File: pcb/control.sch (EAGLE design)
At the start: 74 parts, among them J1 USB-C, J101 MICROSD, J2 2X5, J301 PCC-SMP, J302 3X1_2.54, J304 PCC-SMP, J306 4P-PC-FAN, J307 2X1_2.54, M201 HM-11, Q201 BC817-40, Q202 BC817-40, Q305 BC817-40, Q306 BC817-40, U1 EFM32GG11B4XX_QFN64, U102 SST26VF064B, U2 74LVC1G17, U204 ER-TFT035-6BOT, U205 CP2102N, U301 MCP9600, U302 MCP9600, Y101 8MHz, Y102 32.768KHz

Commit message: pcb v2 done
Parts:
- removed B201: (no value), Eletromechanical > Buzzer:PKLCS1212E2400-R1
- removed C101, C102, C103, C104, C105, C110, C111, C205, C206, C208, C301, C302, C303: 100n, Passive Components > Capacitors > Multilayer Ceramic Capacitors MLCC:MLCC0603
- removed C106, C108, C109: 1u, Passive Components > Capacitors > Multilayer Ceramic Capacitors MLCC:MLCC0603
- removed C207, C209: (no value), Passive Components > Capacitors > Multilayer Ceramic Capacitors MLCC:MLCC0603
- removed D207, D208, D209: LED0603, Opto-electronics > LED Emitters:LED0603
- removed J101: MICROSD, Connectors > card socket:MICROSD
- removed J301, J304: PCC-SMP, Connectors > Other:PCC-SMP
- removed J302: 3X1_2.54, Connectors > Header:3X1_2.54
- removed J306: 4P-PC-FAN, Thermal Management > Fans & Blowers:4P-PC-FAN
- removed J307: 2X1_2.54, Connectors > Header:2X1_2.54
- removed M201: HM-11, Embedded > BLE Module:HM-11
- removed Q201, Q202, Q305, Q306: BC817-40, Semiconductors > Discrete Semiconductors > Transistors > Bipolar Transistors - BJT:BC817-40
- removed R101, R102, R103, R104: 4k7, Passive Components > Resistors > Chip Resistors:RESISTOR0603
- removed R105, R106: (no value), Passive Components > Resistors > Chip Resistors:RESISTOR0603
- removed R203, R212, R318, R319: 1k, Passive Components > Resistors > Chip Resistors:RESISTOR0603
- removed R204, R205, R209, R210, R211: 220, Passive Components > Resistors > Chip Resistors:RESISTOR0603
- removed R206, R213, R320, R321, R326: 100k, Passive Components > Resistors > Chip Resistors:RESISTOR0603
- removed R207: 22.1k, Passive Components > Resistors > Chip Resistors:RESISTOR0603
- removed R208: 47.5k, Passive Components > Resistors > Chip Resistors:RESISTOR0603
- removed R214, R323: 100, Passive Components > Resistors > Chip Resistors:RESISTOR0603
- removed R317: 33k, Passive Components > Resistors > Chip Resistors:RESISTOR0603
- removed SW101: (no value), Eletromechanical > Switches > Tactile Switches:PUSH_BUTTON
- removed U102: SST26VF064B, Semiconductors > Integrated Circuits - ICs > Memory ICs > Flash:SST26VF064B
- removed U204: ER-TFT035-6BOT, Opto-electronics > Displays:ER-TFT035-6BOT
- removed U205: CP2102N, Semiconductors > Integrated Circuits - ICs > Interface ICs > USB Interface IC:CP2102N
- removed U301, U302: MCP9600, Sensors > Temperature Sensors:MCP9600
- removed Y101: 8MHz, Passive Components > Frequency Control & Timing Devices > Crystals:CRYSTALNX5032GA
- removed Y102: 32.768KHz, Passive Components > Frequency Control & Timing Devices > Crystals:CRYSTALCM200S
- added B1: (no value), Eletromechanical > Buzzer:PKLCS1212E2400-R1
- added C1, C4: 10u, Passive Components > Capacitors > Multilayer Ceramic Capacitors MLCC:MLCC0603_MINI
- added C10, C12, C13, C16, C17, C18, C19, C2, C20, C22, C23, C24, C3, C5, C8, C9: 100n, Passive Components > Capacitors > Multilayer Ceramic Capacitors MLCC:MLCC0603
- added C11: (no value), Passive Components > Capacitors > Aluminium Electrolytic Capacitors:CAPACITOR_ELD
- added C14, C15: (no value), Passive Components > Capacitors > Multilayer Ceramic Capacitors MLCC:MLCC0603
- added C25: 4u7, Passive Components > Capacitors > Multilayer Ceramic Capacitors MLCC:MLCC0603
- added C26: 10u, Passive Components > Capacitors > Multilayer Ceramic Capacitors MLCC:MLCC0603
- added C27: 1u, Passive Components > Capacitors > Multilayer Ceramic Capacitors MLCC:MLCC0603
- added C6: 220u, Passive Components > Capacitors > Aluminium Electrolytic Capacitors:CAPACITOR_ELD
- added C7: 470p, Passive Components > Capacitors > Multilayer Ceramic Capacitors MLCC:MLCC0603
- added D10, D11, D12, D13, D14, D7, D8, D9: SK9822, Opto-electronics > LED Emitters:SK9822
- added D2, D5, D6: LED0603, Opto-electronics > LED Emitters:LED0603
- added D3: SMAJ36A, Circuit Protection > ESD Suppressors \ TVS Diodes:SMAJ36A
- added D4: SP0503BAHT, Circuit Protection > ESD Suppressors \ TVS Diodes:SP0503BAHT
- added GND: (no value), Circuit Protection > Resettable Fuses - PPTC:PTC1812
- added J10: USB-C, Connectors > USB:USB-C
- added J3: PCC-SMP, Connectors > Other:PCC-SMP
- added J4: MICROSD, Connectors > card socket:MICROSD
- added J5, J8, J9: 2EDG-2P, Connectors > Other:2EDG-2P
- added J6: 3X1_2.54, Connectors > Header:3X1_2.54
- added J7: 4P-PC-FAN, Thermal Management > Fans & Blowers:4P-PC-FAN
- added L1: 6.8uH, Passive Components > Inductors, Chokes & Coils:INDUCTOR_1207
- added M1: HM-11, Embedded > BLE Module:HM-11
- added Q1, Q2, Q3, Q4: BC817-40, Semiconductors > Discrete Semiconductors > Transistors > Bipolar Transistors - BJT:BC817-40
- added R10, R24, R26, R29, R32: 220, Passive Components > Resistors > Chip Resistors:RESISTOR0603
- added R11, R3: (no value), Passive Components > Resistors > Chip Resistors:RESISTOR0603
- added R12, R13, R14, R15: 4k7, Passive Components > Resistors > Chip Resistors:RESISTOR0603
- added R16: 33k, Passive Components > Resistors > Chip Resistors:RESISTOR0603
- added R17, R18, R19, R25, R27: 1k, Passive Components > Resistors > Chip Resistors:RESISTOR0603
- added R20, R21, R22, R28, R35, R5: 100k, Passive Components > Resistors > Chip Resistors:RESISTOR0603
- added R23, R4: 100, Passive Components > Resistors > Chip Resistors:RESISTOR0603
- added R30: 22.1k, Passive Components > Resistors > Chip Resistors:RESISTOR0603
- added R31: 47.5k, Passive Components > Resistors > Chip Resistors:RESISTOR0603
- added R33, R34: 5.1k, Passive Components > Resistors > Chip Resistors:RESISTOR0603
- added R6: 3k01, Passive Components > Resistors > Chip Resistors:RESISTOR0603
- added R7: 953, Passive Components > Resistors > Chip Resistors:RESISTOR0603
- added R8: 300k, Passive Components > Resistors > Chip Resistors:RESISTOR0603
- added R9: 47k, Passive Components > Resistors > Chip Resistors:RESISTOR0603
- added SW1: (no value), Eletromechanical > Switches > Tactile Switches:PUSH_BUTTON
- added U10: EFM32GG11B4XX_Q100, Semiconductors > Embedded Processors & Controllers > Microcontrollers - MCU:EFM32GG11B4XX_Q100
- added U3: SST26VF064B, Semiconductors > Integrated Circuits - ICs > Memory ICs > Flash:SST26VF064B
- added U4: MCP9600, Sensors > Temperature Sensors:MCP9600
- added U5, U8, U9: 74LVC1G17, Semiconductors > Integrated Circuits - ICs > Logic ICs > Logic Gates:74LVC1G17
- added U6: CP2102N, Semiconductors > Integrated Circuits - ICs > Interface ICs > USB Interface IC:CP2102N
- added U7: ER-TFT035-6BOT, Opto-electronics > Displays:ER-TFT035-6BOT
- added Y1: 8MHz, Passive Components > Frequency Control & Timing Devices > Crystals:CRYSTALNX5032GA
- added Y2: 32.768KHz, Passive Components > Frequency Control & Timing Devices > Crystals:CRYSTALCM200S
- D1: value SP0503BAHT -> SK54L; device Circuit Protection > ESD Suppressors \ TVS Diodes:SP0503BAHT -> Semiconductors > Discrete Semiconductors > Diodes & Rectifiers > Schottky Diodes & Rectifiers:SK54L
- J1: value USB-C -> PCC-SMP; device Connectors > USB:USB-C -> Connectors > Other:PCC-SMP
- J2: value 2X5 -> 2X1_2.54; device Connectors > Header > Shrouded:2X5 -> Connectors > Header:2X1_2.54
- R1: value 1k -> 10M
- U1: value EFM32GG11B4XX_QFN64 -> MIC4682; device Semiconductors > Embedded Processors & Controllers > Microcontrollers - MCU:EFM32GG11B4XX_QFN64 -> Power > Switching Controllers:MIC4682
- U2: value 74LVC1G17 -> MCP9600; device Semiconductors > Integrated Circuits - ICs > Logic ICs > Logic Gates:74LVC1G17 -> Sensors > Temperature Sensors:MCP9600
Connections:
- new net !5V-ERR: U10.PD2
- new net 5V-SENSE: U10.PD4
- new net N$10: D8.SDO@1, D9.SDI@3
- new net N$11: D8.CLKO@6, D9.CLKI@4
- new net N$12: D10.SDI@3, D9.SDO@1
- new net N$14: D10.CLKI@4, D9.CLKO@6
- new net N$20: D10.SDO@1, D11.SDI@3
- new net N$21: D10.CLKO@6, D11.CLKI@4
- new net N$22: D11.SDO@1, D12.SDI@3
- new net N$23: D11.CLKO@6, D12.CLKI@4
- new net N$24: D12.SDO@1, D13.SDI@3
- new net N$26: D12.CLKO@6, D13.CLKI@4
- new net N$27: D13.SDO@1, D14.SDI@3
- new net N$28: D13.CLKO@6, D14.CLKI@4
- new net N$30: GND.2, J5.1.S
- new net N$31: D1.C, L1.P$1, U1.SW
- new net N$32: R6.P$1, R7.P$2, U1.FB
- new net N$34: R1.P$1, R2.P$2, U1.ISET
- new net N$5: J10.CC1@A5, R33.P$2
- new net N$6: D7.SDO@1, D8.SDI@3
- new net N$7: D7.CLKI@4, U9.1.Y
- new net N$8: D7.SDI@3, U8.1.Y
- new net N$9: D7.CLKO@6, D8.CLKI@4
- new net US0-LED-MOSI: U10.PE7, U8.1.A
- new net US0-LED-SCK: U10.PE5, U9.1.A
- new net VIN-SENSE: C7.P$1, R8.P$1, R9.P$2, U10.PD0
- net !RESET: now also SW1.1, SW1.2, U10.!RESET; no longer SW101.1, SW101.2, U1.!RESET@20
- net !TFT_RESET: now also U10.PB5, U7.!RESET; no longer U204.!RESET
- net !TTFT-IRQ: now also U10.PB3, U7.X-/!IRQ!; no longer U204.X-/!IRQ!
- net !TTFT-RST: now also U10.PB6, U7.Y-/!RST!; no longer U204.Y-/!RST!
- net 12V: now also C1.P$1, C11.AN, D3.C, GND.1, J7-12VDC.S, R1.P$2, R22.P$2, R8.P$2, U1.IN; no longer J2-1.S, J2-3.S, J306-12VDC.S, R321.P$2
- net 3.3V: now also C10.P$1, C12.P$1, C13.P$1, C14.P$1, C15.P$1, C16.P$1, C17.P$1, C18.P$1, C19.P$1, C2.P$1, C20.P$1, C22.P$1, C24.P$1, C25.P$1, C5.P$1, C8.P$1, C9.P$1, J4.4, M1.VCC@9, R11.P$2, R12.P$2, R13.P$2, R14.P$2, R15.P$2, R24.P$1, R26.P$1, R28.P$2, R3.P$2, R35.P$2, R5.P$2, U10.AVDD@0, U10.AVDD@1, U10.DVDD, U10.IOVDD0@0, U10.IOVDD0@1, U10.IOVDD0@2, U10.IOVDD0@3, U10.IOVDD0@4, U10.VREGO, U2.VDD@8, U3.VCC, U4.ADDR@16, U4.VDD@8, U6.VDD@6, U6.VIO@5, U6.VREGIN@7, U7.!RD, U7.IM0, U7.IM1, U7.IM2, U7.VCI, U7.VDDI@0, U7.VDDI@1; no longer C101.P$1, C102.P$1, C103.P$1, C104.P$1, C105.P$1, C106.P$1, C110.P$1, C111.P$1, C205.P$1, C206.P$1, C207.P$1, C208.P$1, C209.P$1, C301.P$1, C302.P$1, J101.4, M201.VCC@9, R101.P$2, R102.P$2, R103.P$2, R104.P$2, R105.P$2, R106.P$2, R206.P$2, R209.P$1, R210.P$1, R326.P$2, U1.AVDD@23, U1.AVDD@27, U1.DVDD@39, U1.IOVDD0@26, U1.IOVDD0@55, U1.IOVDD0@8, U1.VREGO@46, U102.VCC, U204.!RD, U204.IM0, U204.IM1, U204.IM2, U204.VCI, U204.VDDI@0, U204.VDDI@1, U205.VDD@6, U205.VIO@5, U205.VREGIN@7, U301.VDD@8, U302.ADDR@16, U302.VDD@8
- net 5V: now also C23.P$1, C26.P$1, C4.P$1, C6.AN, D10.VDD@5, D11.VDD@5, D12.VDD@5, D13.VDD@5, D14.VDD@5, D7.VDD@5, D8.VDD@5, D9.VDD@5, J6-2.S, L1.P$2, R21.P$2, R23.P$2, R6.P$2, U10.VBUS, U10.VREGI, U5.PW.VCC, U7.LEDA, U8.PW.VCC, U9.PW.VCC; no longer C108.P$1, J2-5.S, J2-7.S, J302-2.S, R213.P$2, R214.P$2, U1.VBUS@52, U1.VREGI@45, U2.PW.VCC, U204.LEDA
- net BLE-!RST: now also M1.!RST!@11, U10.PE0; no longer M201.!RST!@11
- net BLE-KEY: now also M1.PIO0@16, U10.PE1; no longer M201.PIO0@16
- net DECOUPLE: now also C27.P$1, U10.DECOUPLE; no longer C109.P$1, U1.DECOUPLE@40
- net DOOR-SW: now also C3.P$1, R4.P$2, U10.PC7; no longer C303.P$1, R323.P$2
- net GND: now also C1.P$2, C10.P$2, C11.CA, C12.P$2, C13.P$2, C14.P$2, C15.P$2, C16.P$2, C17.P$2, C18.P$2, C19.P$2, C2.P$2, C20.P$2, C22.P$2, C23.P$2, C24.P$2, C25.P$2, C26.P$2, C27.P$2, C3.P$2, C4.P$2, C5.P$2, C6.CA, C7.P$2, C8.P$2, C9.P$2, D1.A, D10.GND@2, D11.GND@2, D12.GND@2, D13.GND@2, D14.GND@2, D2.CA, D3.A, D4.1, D7.GND@2, D8.GND@2, D9.GND@2, J1.BAR.S, J10.GND@A12,A1,B1,B12, J3.BAR.S, J4.6, J4.BODY@10, J5.2.S, J6-3.S, J8.2.S, J9.2.S, M1.GND@12, Q1.EM2, Q2.EM2, Q3.EM2, Q4.EM2, R16.P$1, R25.P$1, R31.P$1, R33.P$1, R34.P$1, R7.P$1, R9.P$1, SW1.3, SW1.4, U1.GND@1, U1.GND@2, U1.GND@3, U1.SHDN, U10.VSS@0, U10.VSS@1, U10.VSS@2, U10.VSS@3, U2.ADDR@16, U2.EP, U2.GND@1, U2.GND@10, U2.GND@13, U2.GND@17, U2.GND@18, U2.GND@3, U2.GND@5, U2.GND@6, U2.GND@7, U2.GND@9, U3.GND, U4.EP, U4.GND@1, U4.GND@10, U4.GND@13, U4.GND@17, U4.GND@18, U4.GND@3, U4.GND@5, U4.GND@6, U4.GND@7, U4.GND@9, U5.PW.GND, U6.GND@2, U6.GND@PAD, U7.DB0, U7.DB1, U7.DB10, U7.DB11, U7.DB12, U7.DB13, U7.DB14, U7.DB15, U7.DB16, U7.DB17, U7.DB2, U7.DB3, U7.DB4, U7.DB5, U7.DB6, U7.DB7, U7.DB8, U7.DB9, U7.DE, U7.DOTCLK, U7.GND@0, U7.GND@1, U7.GND@2, U7.GND@3, U7.HSYNC, U7.TE, U7.VSYNC, U8.PW.GND, U9.PW.GND; no longer C101.P$2, C102.P$2, C103.P$2, C104.P$2, C105.P$2, C106.P$2, C108.P$2, C109.P$2, C110.P$2, C111.P$2, C205.P$2, C206.P$2, C207.P$2, C208.P$2, C209.P$2, C301.P$2, C302.P$2, C303.P$2, D1.1, D208.CA, J1.GND@A12,A1,B1,B12, J101.6, J101.BODY@10, J2-4.S, J2-6.S, J2-8.S, J301.BAR.S, J302-3.S, J304.BAR.S, J307-2.S, M201.GND@12, Q201.EM2, Q202.EM2, Q305.EM2, Q306.EM2, R1.P$1, R208.P$1, R317.P$1, SW101.3, SW101.4, U1.VSS@65, U102.GND, U2.PW.GND, U204.DB0, U204.DB1, U204.DB10, U204.DB11, U204.DB12, U204.DB13, U204.DB14, U204.DB15, U204.DB16, U204.DB17, U204.DB2, U204.DB3, U204.DB4, U204.DB5, U204.DB6, U204.DB7, U204.DB8, U204.DB9, U204.DE, U204.DOTCLK, U204.GND@0, U204.GND@1, U204.GND@2, U204.GND@3, U204.HSYNC, U204.TE, U204.VSYNC, U205.GND@2, U205.GND@PAD, U301.ADDR@16, U301.EP, U301.GND@1, U301.GND@10, U301.GND@13, U301.GND@17, U301.GND@18, U301.GND@3, U301.GND@5, U301.GND@6, U301.GND@7, U301.GND@9, U302.EP, U302.GND@1, U302.GND@10, U302.GND@13, U302.GND@17, U302.GND@18, U302.GND@3, U302.GND@5, U302.GND@6, U302.GND@7, U302.GND@9
- net I2C0-SCL-SENS: now also R13.P$1, U10.PD7, U2.SCL@19, U4.SCL@19; no longer R102.P$1, U301.SCL@19, U302.SCL@19
- net I2C0-SDA-SENS: now also R12.P$1, U10.PD6, U2.SDA@20, U4.SDA@20; no longer R101.P$1, U301.SDA@20, U302.SDA@20
- net I2C1-SCL-TTFT: now also R15.P$1, U10.PB12, U7.X+/SCL; no longer R104.P$1, U204.X+/SCL
- net I2C1-SDA-TTFT: now also R14.P$1, U10.PB11, U7.Y+/SDA; no longer R103.P$1, U204.Y+/SDA
- net MAIN_HFXTAL_N: now also U10.PB13, Y1.1; no longer Y101.1
- net MAIN_HFXTAL_P: now also U10.PB14, Y1.2; no longer Y101.2
- net MAIN_LFXTAL_N: now also U10.PB8, Y2.2; no longer Y102.2
- net MAIN_LFXTAL_P: now also U10.PB7, Y2.1; no longer Y102.1
- net N$1: now also J2-1.S, R4.P$1, R5.P$1; no longer J307-1.S, R323.P$1, R326.P$1
- net N$13: now also D5.CA, U6.GPIO1-RXT@13; no longer D207.CA, U205.GPIO1-RXT@13
- net N$15: now also D6.CA, U6.GPIO0-TXT@14; no longer D209.CA, U205.GPIO0-TXT@14
- net N$16: now also D6.AN, R26.P$2; no longer D209.AN, R210.P$2
- net N$17: now also B1.B, Q1.C03, R21.P$1; no longer B201.B, Q202.C03, R213.P$1
- net N$18: now also Q1.BA1, R17.P$2; no longer Q202.BA1, R212.P$2
- net N$19: now also D5.AN, R24.P$2; no longer D207.AN, R209.P$2
- net N$2: now also J6-1.S, U5.1.Y; no longer J302-1.S, U2.1.Y
- net N$25: now also Q4.BA1, R27.P$2; no longer Q201.BA1, R203.P$2
- net N$3: now also J10.CC2@B5, R34.P$2; no longer J1.CC@A5,B5, R2.P$2
- net N$35: now also D2.AN, R10.P$2; no longer D208.AN, R211.P$2
- net N$36: now also M1.PIO1@15, R10.P$1; no longer M201.PIO1@15, R211.P$1
- net N$4: now also B1.A, R23.P$1; no longer B201.A, R214.P$1
- net N$56: now also Q3.BA1, R19.P$2; no longer Q306.BA1, R319.P$2
- net N$57: now also J7-GND.S, Q3.C03; no longer J306-GND.S, Q306.C03
- net N$58: now also Q2.BA1, R18.P$2; no longer Q305.BA1, R318.P$2
- net N$59: now also J7-CTRL.S, Q2.C03, R22.P$1; no longer J306-CTRL.S, Q305.C03, R321.P$1
- net N$64: now also J7-SENSE.S, R20.P$2; no longer J306-SENSE.S, R320.P$2
- net PRS-CH11-SSR-OUT: now also J9.1.S, U10.PD5; no longer J2-9.S
- net QSPI_CLK: now also U10.PF6, U3.SCK; no longer U102.SCK
- net QSPI_CS0: now also R3.P$1, U10.PF7, U3.!CS!; no longer R105.P$1, U102.!CS!
- net QSPI_D0: now also U10.PD9, U3.MOSI/IO0; no longer U102.MOSI/IO0
- net QSPI_D1: now also U10.PD10, U3.MISO/IO1; no longer U102.MISO/IO1
- net QSPI_D2: now also U10.PD11, U3.!WP!/IO2; no longer U102.!WP!/IO2
- net QSPI_D3: now also U10.PD12, U3.!HOLD!/IO3; no longer U102.!HOLD!/IO3
- net SDIO-CD: now also J4.CD@9, R11.P$1, U10.PF8; no longer J101.CD@9, R106.P$1
- net SDIO-CLK: now also J4.5, U10.PE13; no longer J101.5
- net SDIO-CMD: now also J4.3, U10.PE12; no longer J101.3
- net SDIO-DAT0: now also J4.7, U10.PE11; no longer J101.7
- net SDIO-DAT1: now also J4.8, U10.PE10; no longer J101.8
- net SDIO-DAT2: now also J4.1, U10.PE9; no longer J101.1
- net SDIO-DAT3: now also J4.2, U10.PE8; no longer J101.2
- net SWCLK: now also U10.PF0
- net SWDIO: now also U10.PF1
- net SWO: now also U10.PF2
- net TC_VIN0+: now also J1.T+.S, U2.VIN+@2; no longer J301.T+.S, U301.VIN+@2
- net TC_VIN0-: now also J1.T-.S, U2.VIN-@4; no longer J301.T-.S, U301.VIN-@4
- net TC_VIN1+: now also J3.T+.S, U4.VIN+@2; no longer J304.T+.S, U302.VIN+@2
- net TC_VIN1-: now also J3.T-.S, U4.VIN-@4; no longer J304.T-.S, U302.VIN-@4
- net TFT-DC: now also U10.PC1, U7.D/!C!; no longer U204.D/!C!
- net TFT-LEDK: now also Q4.C03, R29.P$1, R32.P$1; no longer Q201.C03, R204.P$1, R205.P$1
- net TFT-LEDK1: now also R29.P$2, U7.LEDK@0; no longer R204.P$2, U204.LEDK@0
- net TFT-LEDK2: now also R32.P$2, U7.LEDK@1; no longer R205.P$2, U204.LEDK@1
- net TIM0-CC2-BUZZ: now also R17.P$1, U10.PA8; no longer R212.P$1
- net TIM1-CC0-TFT-BL: now also R25.P$2, R27.P$1, U10.PB0; no longer R1.P$2, R203.P$1
- net TIM2-CC2FAN0-SNSE: now also R16.P$2, R20.P$1, U10.PC10; no longer R317.P$2, R320.P$1
- net TIM5-CC0-FAN0-GND: now also R19.P$1, U10.PC8; no longer R319.P$1
- net TIM5-CC1-FAN0-CTRL: now also R18.P$1, U10.PC9; no longer R318.P$1
- net U0RX-USB-TX: now also U10.PA4, U6.TXD@21; no longer U205.TXD@21
- net U0TX-USB-RX: now also U10.PA3, U6.RXD@20; no longer U205.RXD@20
- net U1RX-BLE-TX: now also M1.TX@2, U10.PE3; no longer M201.TX@2
- net U1TX-BLE-RX: now also M1.RX@4, U10.PE2; no longer M201.RX@4
- net UART_VBUS: now also R30.P$1, R31.P$2, U6.VBUS@8; no longer R207.P$1, R208.P$2, U205.VBUS@8
- net US2-CLK-TFT: now also U10.PC4, U7.!WR!/SCL; no longer U204.!WR!/SCL
- net US2-CS-TFT: now also R35.P$1, U10.PC5, U7.!CS; no longer R206.P$1, U204.!CS
- net US2-MISO-TFT: now also U10.PC3, U7.SDO; no longer U204.SDO
- net US2-MOSI-TFT: now also U10.PC2, U7.SDA; no longer U204.SDA
- net USB-RST: now also U10.PA2, U6.RSTB@9; no longer U205.RSTB@9
- net USB-SUS: now also U10.PA1, U6.SUSPEND@17; no longer U205.SUSPEND@17
- net USB-UART-D+: now also D4.3, J10.DP@A6,B6, U6.D+@3; no longer D1.3, J1.DP@A6,B6, U205.D+@3
- net USB-UART-D-: now also D4.2, J10.DN@A7,B7, U6.D-@4; no longer D1.2, J1.DN@A7,B7, U205.D-@4
- net V_USB: now also D4.4, J10.VBUS@B9,B4,A4,A9, R30.P$2; no longer D1.4, J1.VBUS@B9,B4,A4,A9, R207.P$2
- net WTIM1-CC1-ZERO-CROSS: now also J8.1.S, R28.P$1, U10.PE4; no longer J2-10.S
- net WTIM2-CC0-SERVO0-SIG: now also U10.PD3, U5.1.A; no longer U2.1.A

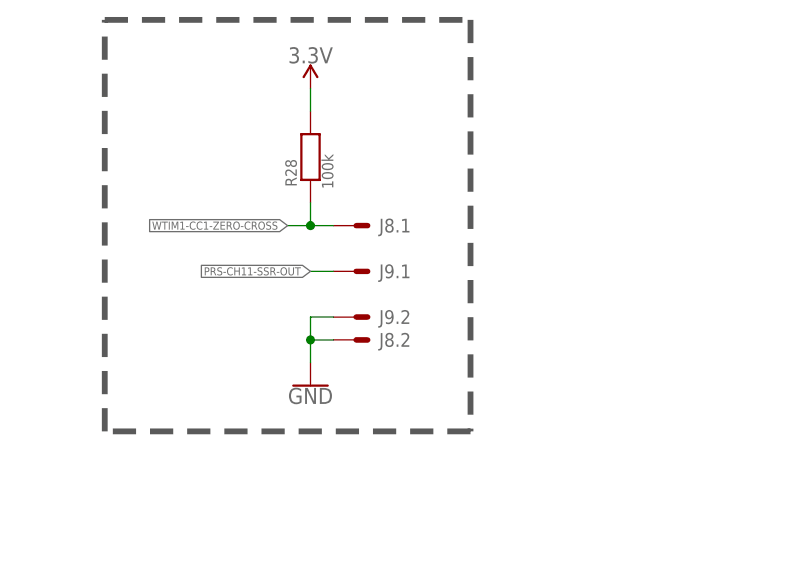
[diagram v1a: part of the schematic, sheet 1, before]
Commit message: finished silkscreen and ssr pcb
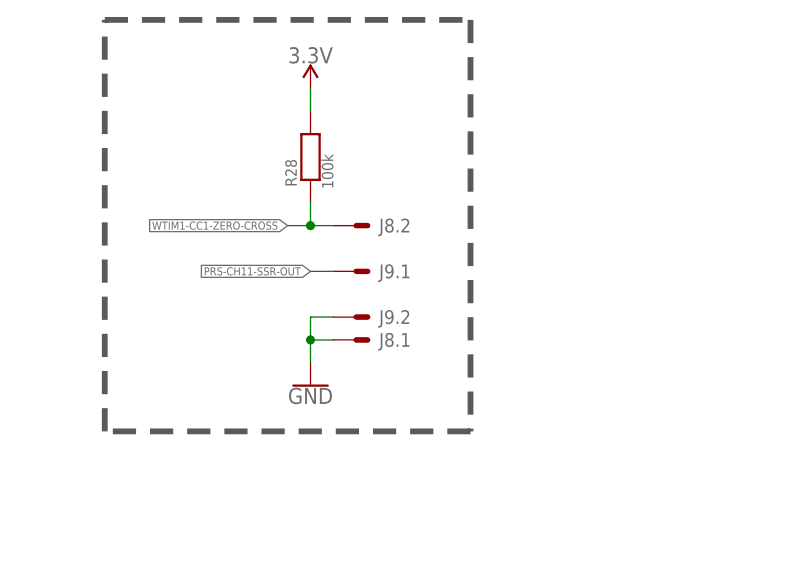
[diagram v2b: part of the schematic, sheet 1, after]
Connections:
- net GND: now also J8.1.S; no longer J8.2.S
- net WTIM1-CC1-ZERO-CROSS: now also J8.2.S; no longer J8.1.S
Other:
- moved on the sheet: J8.1, J8.2
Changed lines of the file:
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@@
 <attribute name="VALUE" x="462.28" y="-50.546" size="1.778" layer="96" align="bottom-center"/>
 </instance>
-<instance part="J8" gate=".1" x="612.14" y="-66.04" smashed="yes">
+<instance part="J8" gate=".1" x="612.14" y="-78.74" smashed="yes">
+<attribute name="NAME" x="614.68" y="-79.502" size="1.524" layer="95"/>
+</instance>
+<instance part="J8" gate=".2" x="612.14" y="-66.04" smashed="yes">
 <attribute name="NAME" x="614.68" y="-66.802" size="1.524" layer="95"/>
-</instance>
-<instance part="J8" gate=".2" x="612.14" y="-78.74" smashed="yes">
-<attribute name="NAME" x="614.68" y="-79.502" size="1.524" layer="95"/>
 </instance>
 <instance part="J9" gate=".1" x="612.14" y="-71.12" smashed="yes">
@@
 <pinref part="J9" gate=".2" pin="S"/>
 <wire x1="609.6" y1="-76.2" x2="607.06" y2="-76.2" width="0.1524" layer="91"/>
-<pinref part="J8" gate=".2" pin="S"/>
+<wire x1="607.06" y1="-76.2" x2="607.06" y2="-78.74" width="0.1524" layer="91"/>
+<pinref part="GND41" gate="1" pin="GND"/>
+<pinref part="J8" gate=".1" pin="S"/>
+<wire x1="607.06" y1="-78.74" x2="607.06" y2="-81.28" width="0.1524" layer="91"/>
 <wire x1="609.6" y1="-78.74" x2="607.06" y2="-78.74" width="0.1524" layer="91"/>
-<wire x1="607.06" y1="-78.74" x2="607.06" y2="-81.28" width="0.1524" layer="91"/>
-<wire x1="607.06" y1="-76.2" x2="607.06" y2="-78.74" width="0.1524" layer="91"/>
 <junction x="607.06" y="-78.74"/>
-<pinref part="GND41" gate="1" pin="GND"/>
 </segment>
 <segment>
@@
 <segment>
 <label x="604.52" y="-66.04" size="0.889" layer="95" rot="R180" xref="yes"/>
-<wire x1="609.6" y1="-66.04" x2="607.06" y2="-66.04" width="0.1524" layer="91"/>
-<pinref part="J8" gate=".1" pin="S"/>
 <pinref part="R28" gate="G$1" pin="P$1"/>
 <wire x1="607.06" y1="-66.04" x2="604.52" y2="-66.04" width="0.1524" layer="91"/>
 <wire x1="607.06" y1="-63.5" x2="607.06" y2="-66.04" width="0.1524" layer="91"/>
+<pinref part="J8" gate=".2" pin="S"/>
+<wire x1="609.6" y1="-66.04" x2="607.06" y2="-66.04" width="0.1524" layer="91"/>
 <junction x="607.06" y="-66.04"/>
 </segment>

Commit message: pcb order
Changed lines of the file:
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@@
 <?xml version="1.0" encoding="utf-8"?>
 <!DOCTYPE eagle SYSTEM "eagle.dtd">
-<eagle version="9.3.2">
+<eagle version="9.3.0">
 <drawing>
 <settings>
@@
 </nets>
 </sheet>
-<sheet>
-<plain>
-</plain>
-<instances>
-</instances>
-<busses>
-</busses>
-<nets>
-</nets>
-</sheet>

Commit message: sync
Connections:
- new net TIM0-CC0-BUZZ: U10.PA8
- net TIM0-CC2-BUZZ: no longer U10.PA8
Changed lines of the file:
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@@
 <pinref part="R17" gate="G$1" pin="P$1"/>
-</segment>
-<segment>
-<wire x1="172.72" y1="193.04" x2="170.18" y2="193.04" width="0.1524" layer="91"/>
-<label x="170.18" y="193.04" size="0.8128" layer="95" rot="R180" xref="yes"/>
-<pinref part="U10" gate="G$1" pin="PA8"/>
 </segment>
 </net>
@@
 </segment>
 </net>
+<net name="TIM0-CC0-BUZZ" class="0">
+<segment>
+<wire x1="172.72" y1="193.04" x2="170.18" y2="193.04" width="0.1524" layer="91"/>
+<label x="170.18" y="193.04" size="0.8128" layer="95" rot="R180" xref="yes"/>
+<pinref part="U10" gate="G$1" pin="PA8"/>
+</segment>
+</net>
